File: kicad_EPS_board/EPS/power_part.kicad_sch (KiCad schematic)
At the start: 25 parts, among them Q1 BSC016N06NS, Q2 BSC016N06NS, Q3 BSC016N06NS, Q4 BSC016N06NS, Q5 BSS138

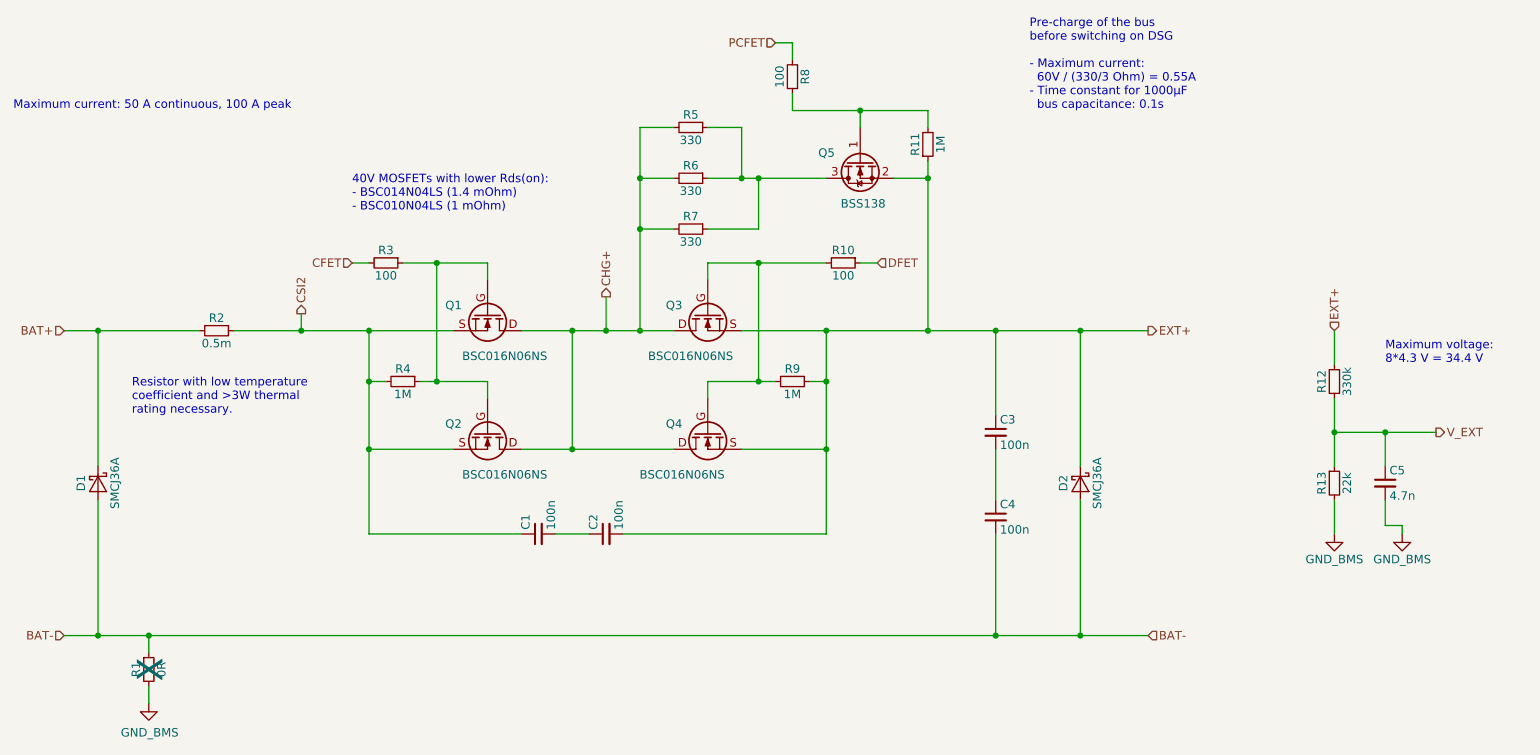
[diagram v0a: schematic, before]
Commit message: kicad EPS board V2 revision and already generated html doc files
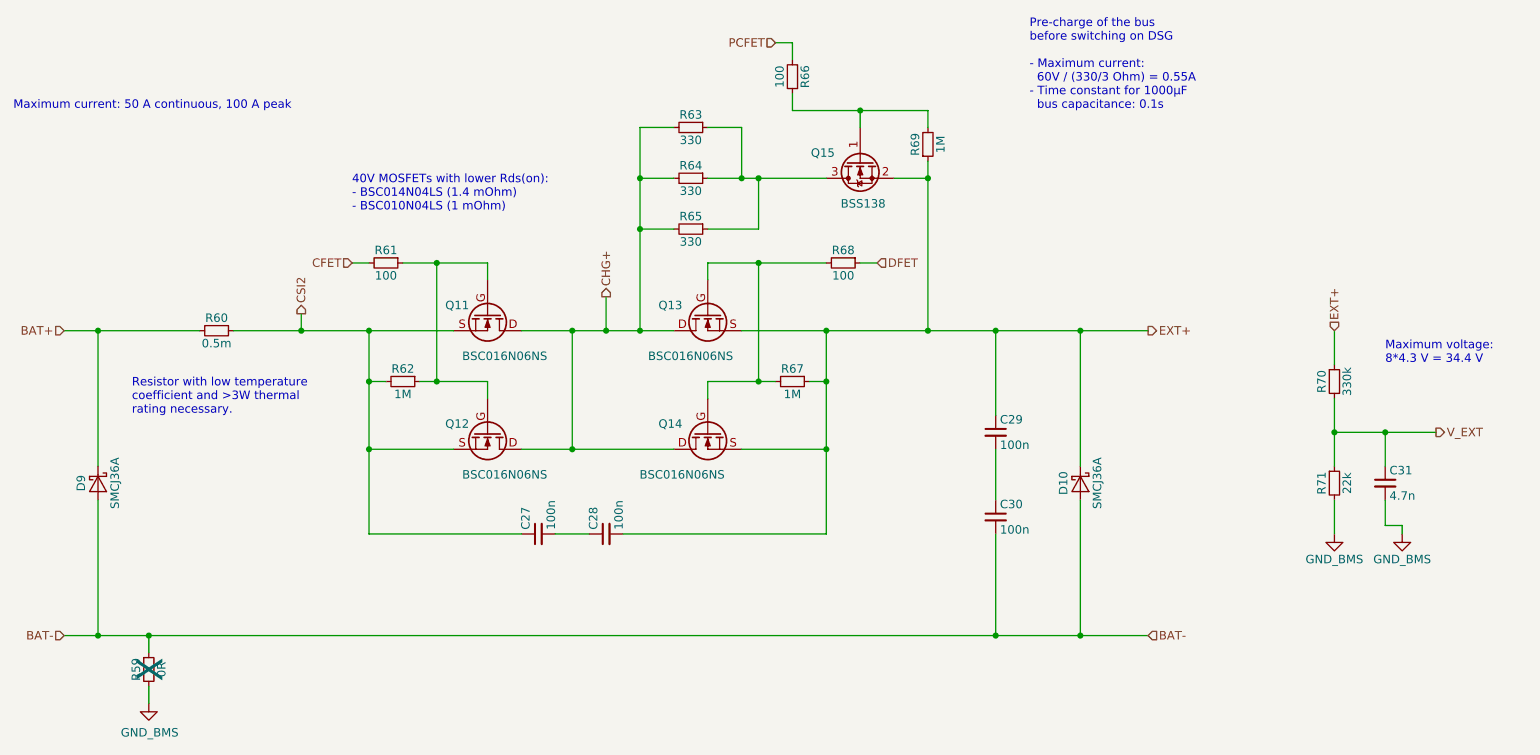
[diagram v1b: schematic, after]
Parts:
- renumbered C1 to C27, C2 to C28, C3 to C29, C4 to C30, C5 to C31, D2 to D10, D1 to D9, Q1 to Q11, Q2 to Q12, Q3 to Q13, Q4 to Q14, Q5 to Q15, R1 to R59, R2 to R60, R3 to R61, R4 to R62, R5 to R63, R6 to R64, R7 to R65, R8 to R66, R9 to R67, R10 to R68, R11 to R69, R12 to R70, R13 to R71
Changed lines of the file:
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@@
 (kicad_sch
-	(version 20231120)
+	(version 20250114)
 	(generator "eeschema")
-	(generator_version "8.0")
+	(generator_version "9.0")
 	(paper "A4")
+	(text "40V MOSFETs with lower Rds(on):\n- BSC014N04LS (1.4 mOhm)\n- BSC010N04LS (1 mOhm)"
+		(exclude_from_sim no)
+		(at 91.44 71.12 0)
+		(effects
+			(font
+				(size 1.27 1.27)
+			)
+			(justify left bottom)
+		)
+	)
+	(text "Maximum voltage:\n8*4.3 V = 34.4 V"
+		(exclude_from_sim no)
+		(at 246.38 93.98 0)
+		(effects
+			(font
+				(size 1.27 1.27)
+			)
+			(justify left bottom)
+		)
+	)
+	(text "Pre-charge of the bus\nbefore switching on DSG\n\n- Maximum current:\n  60V / (330/3 Ohm) = 0.55A\n- Time constant for 1000µF\n  bus capacitance: 0.1s"
+		(exclude_from_sim no)
+		(at 193.04 55.88 0)
+		(effects
+			(font
+				(size 1.27 1.27)
+			)
+			(justify left bottom)
+		)
+	)
+	(text "Resistor with low temperature\ncoefficient and >3W thermal\nrating necessary."
+		(exclude_from_sim no)
+		(at 58.42 101.6 0)
+		(effects
+			(font
+				(size 1.27 1.27)
+			)
+			(justify left bottom)
+		)
+	)
+	(text "Maximum current: 50 A continuous, 100 A peak"
+		(exclude_from_sim no)
+		(at 40.64 55.88 0)
+		(effects
+			(font
+				(size 1.27 1.27)
+			)
+			(justify left bottom)
+		)
+	)
 	(junction
 		(at 162.56 96.52)
@@
 		)
 	)
-	(text "40V MOSFETs with lower Rds(on):\n- BSC014N04LS (1.4 mOhm)\n- BSC010N04LS (1 mOhm)"
-		(exclude_from_sim no)
-		(at 91.44 71.12 0)
-		(effects
-			(font
-				(size 1.27 1.27)
-			)
-			(justify left bottom)
-		)
-	)
-	(text "Maximum voltage:\n8*4.3 V = 34.4 V"
-		(exclude_from_sim no)
-		(at 246.38 93.98 0)
-		(effects
-			(font
-				(size 1.27 1.27)
-			)
-			(justify left bottom)
-		)
-	)
-	(text "Pre-charge of the bus\nbefore switching on DSG\n\n- Maximum current:\n  60V / (330/3 Ohm) = 0.55A\n- Time constant for 1000µF\n  bus capacitance: 0.1s"
-		(exclude_from_sim no)
-		(at 193.04 55.88 0)
-		(effects
-			(font
-				(size 1.27 1.27)
-			)
-			(justify left bottom)
-		)
-	)
-	(text "Resistor with low temperature\ncoefficient and >3W thermal\nrating necessary."
-		(exclude_from_sim no)
-		(at 58.42 101.6 0)
-		(effects
-			(font
-				(size 1.27 1.27)
-			)
-			(justify left bottom)
-		)
-	)
-	(text "Maximum current: 50 A continuous, 100 A peak"
-		(exclude_from_sim no)
-		(at 40.64 55.88 0)
-		(effects
-			(font
-				(size 1.27 1.27)
-			)
-			(justify left bottom)
-		)
-	)
 	(hierarchical_label "CFET"
 		(shape input)
@@
 		(on_board yes)
 		(dnp no)
-		(property "Reference" "Q1"
+		(property "Reference" "Q11"
 			(at 105.41 85.09 90)
 			(effects
@@
 		(on_board yes)
 		(dnp no)
-		(property "Reference" "C2"
+		(property "Reference" "C28"
 			(at 127.635 118.745 0)
 			(effects
@@
 		(on_board yes)
 		(dnp no)
-		(property "Reference" "Q2"
+		(property "Reference" "Q12"
 			(at 105.41 102.87 90)
 			(effects
@@
 		(on_board yes)
 		(dnp no)
-		(property "Reference" "#PWR02"
+		(property "Reference" "#PWR060"
 			(at 238.76 125.73 0)
 			(effects
@@
 		(on_board yes)
 		(dnp no)
-		(property "Reference" "R12"
+		(property "Reference" "R70"
 			(at 236.855 96.52 90)
 			(effects
@@
 		(on_board yes)
 		(dnp no)
-		(property "Reference" "R7"
+		(property "Reference" "R65"
 			(at 142.24 71.755 90)
 			(effects
@@
 		(on_board yes)
 		(dnp no)
-		(property "Reference" "R11"
+		(property "Reference" "R69"
 			(at 175.895 60.96 90)
 			(effects
@@
 		(on_board yes)
 		(dnp no)
-		(property "Reference" "R6"
+		(property "Reference" "R64"
 			(at 142.24 64.135 90)
 			(effects
@@
 		(on_board yes)
 		(dnp no)
-		(property "Reference" "C5"
+		(property "Reference" "C31"
 			(at 247.015 109.855 0)
 			(effects
@@
 		(on_board yes)
 		(dnp no)
-		(property "Reference" "Q4"
+		(property "Reference" "Q14"
 			(at 140.97 102.87 90)
 			(effects
@@
 		(on_board yes)
 		(dnp no)
-		(property "Reference" "#PWR03"
+		(property "Reference" "#PWR061"
 			(at 248.92 125.73 0)
 			(effects
@@
 		(on_board yes)
 		(dnp no)
-		(property "Reference" "D1"
+		(property "Reference" "D9"
 			(at 50.8 111.76 0)
 			(effects
@@
 		(on_board yes)
 		(dnp no)
-		(property "Reference" "R10"
+		(property "Reference" "R68"
 			(at 165.1 76.835 90)
 			(effects
@@
 		(on_board yes)
 		(dnp no)
-		(property "Reference" "R9"
+		(property "Reference" "R67"
 			(at 157.48 94.615 90)
 			(effects
@@
 		(on_board yes)
 		(dnp no)
-		(property "Reference" "D2"
+		(property "Reference" "D10"
 			(at 198.12 111.76 0)
 			(effects
@@
 		(on_board yes)
 		(dnp no)
-		(property "Reference" "Q5"
+		(property "Reference" "Q15"
 			(at 163.83 62.23 90)
 			(effects
@@
 		(on_board yes)
 		(dnp no)
-		(property "Reference" "R4"
+		(property "Reference" "R62"
 			(at 99.06 94.615 90)
 			(effects
@@
 		(on_board yes)
 		(dnp no)
-		(property "Reference" "R13"
+		(property "Reference" "R71"
 			(at 236.855 111.76 90)
 			(effects
@@
 		(on_board yes)
 		(dnp no)
-		(property "Reference" "Q3"
+		(property "Reference" "Q13"
 			(at 140.97 85.09 90)
 			(effects
@@
 		(on_board yes)
 		(dnp no)
-		(property "Reference" "R2"
+		(property "Reference" "R60"
 			(at 71.12 86.995 90)
 			(effects
@@
 		(on_board yes)
 		(dnp no)
-		(property "Reference" "C1"
+		(property "Reference" "C27"
 			(at 117.475 118.745 0)
 			(effects
@@
 		(on_board yes)
 		(dnp no)
-		(property "Reference" "C4"
+		(property "Reference" "C30"
 			(at 188.595 114.935 0)
 			(effects
@@
 		(on_board yes)
 		(dnp no)
-		(property "Reference" "R3"
+		(property "Reference" "R61"
 			(at 96.52 76.835 90)
 			(effects
@@
 		(on_board yes)
 		(dnp no)
-		(property "Reference" "#PWR01"
+		(property "Reference" "#PWR059"
 			(at 60.96 151.13 0)
 			(effects
@@
 		(on_board yes)
 		(dnp no)
-		(property "Reference" "R8"
+		(property "Reference" "R66"
 			(at 159.385 50.8 90)
 			(effects
@@
 		(on_board yes)
 		(dnp no)
-		(property "Reference" "C3"
+		(property "Reference" "C29"
 			(at 188.595 102.235 0)
 			(effects
@@
 		(on_board yes)
 		(dnp no)
-		(property "Reference" "R5"
+		(property "Reference" "R63"
 			(at 142.24 56.515 90)
 			(effects
@@
 		(on_board yes)
 		(dnp no)
-		(property "Reference" "R1"
+		(property "Reference" "R59"
 			(at 59.055 139.7 90)
 			(effects
